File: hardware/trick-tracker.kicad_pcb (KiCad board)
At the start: 2 copper layers, 23.7 x 49.9 mm, 44 parts, among them J1 USB4105-GF-A, J2 S2B-PH-K, J3 QWiiC, U1 MS88SF2, U2 DPS368XTSA1, U3 LSM9DS1, U4 MCP73831-2-OT, U5 MIC5504-3.3YM5

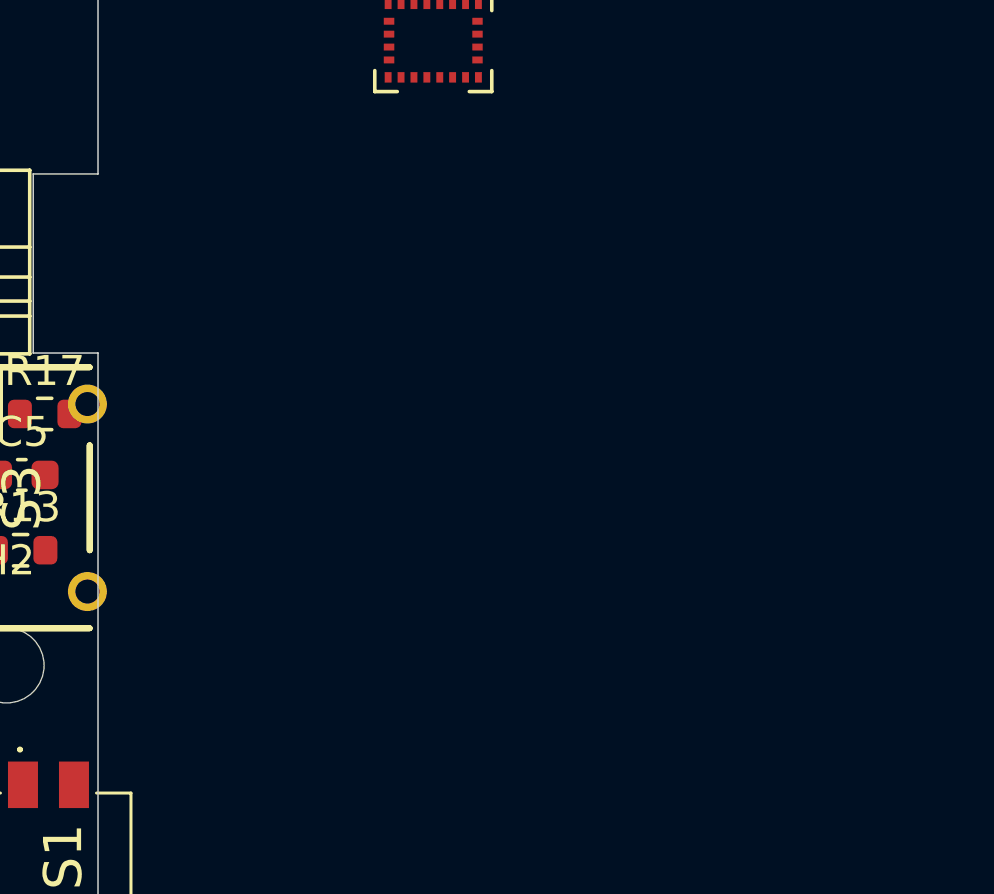
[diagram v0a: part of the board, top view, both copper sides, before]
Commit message: Add Micro SD-Card holder
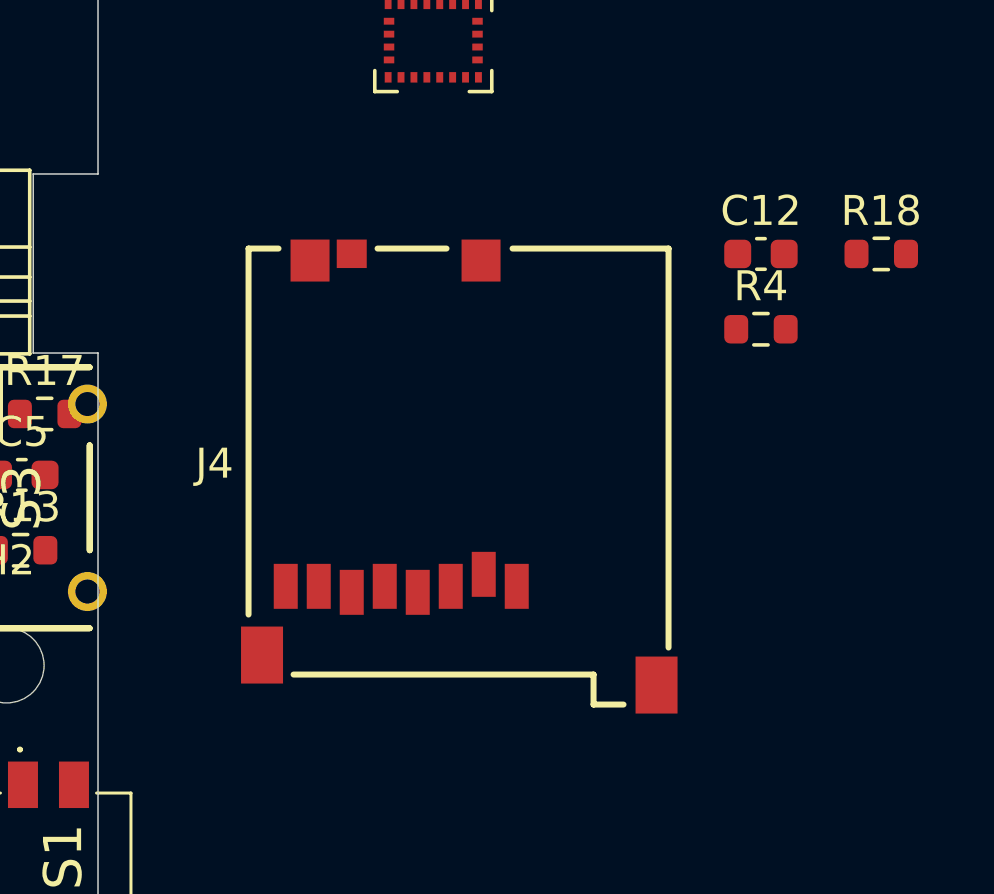
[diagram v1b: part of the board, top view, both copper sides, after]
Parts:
- added C12: 0.1µF, Capacitor_SMD:C_0603_1608Metric, F.Cu at (178.7, 113.0)
- added J4: MEM2051-00-195-00-A, MEM2051-00-195-00-A:GCT_MEM2051-00-195-00-A, F.Cu at (168.6, 120.5)
- added R18: 2M, Resistor_SMD:R_0603_1608Metric, F.Cu at (182.7, 113.0)
- added R4: 806k, Resistor_SMD:R_0603_1608Metric, F.Cu at (178.7, 115.5)
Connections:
- net /CC1 renamed Net-(J1-PadA5)
- net /CC2 renamed Net-(J1-PadB5)
- U1 pad 22: Net-(U1-Pad22) -> /BAT_SENS

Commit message: Moved components
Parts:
- removed LED1: APHF1608LSEEQBDZGKC, APHF1608LSEEQBDZGKC:APHF1608LSEEQBDZGKC
- removed R8: 2k2, Resistor_SMD:R_0603_1608Metric
- removed R9: 390R, Resistor_SMD:R_0603_1608Metric
- added D4: GREEN, LED_SMD:LED_0603_1608Metric, F.Cu at (160.0, 106.7)
- added D5: DSS13UTR, Diode_SMD:D_SOD-123F, F.Cu at (150.0, 122.6)
- added H3: MountingHole, MountingHole:MountingHole_2.5mm, F.Cu at (132.8, 101.3)
- added H4: MountingHole, MountingHole:MountingHole_2.5mm, F.Cu at (158.2, 101.3)
- D1: value MBR120 -> DSS13UTR; footprint Diode_SMD:D_0603_1608Metric -> Diode_SMD:D_SOD-123F
- J4: moved to B.Cu
- R7: value 1k2 -> 470
- U4: value MCP73831-2-OT -> MCP73831/OT
- moved R18 42.5 mm to (140.3, 110.1), turned to 180 degrees
- moved C12 38.6 mm to (140.3, 108.5)
- moved R4 38.5 mm to (140.3, 111.8), turned to 180 degrees
- moved R7 31.2 mm to (158.4, 106.7), turned to 90 degrees
- moved C1 29.6 mm to (152.8, 121.9)
- moved U3 21.5 mm to (146.6, 109.3)
- moved C7 20.2 mm to (149.4, 106.7)
- moved U2 19.5 mm to (135.3, 114.8), turned to 90 degrees
- moved H1 19.3 mm to (132.8, 134.2)
- moved J4 16.8 mm to (152.0, 123.1), turned to 270 degrees
- moved C8 16.3 mm to (146.3, 106.7)
- moved C10 16.1 mm to (132.8, 114.8), turned to 90 degrees
- moved C6 15.4 mm to (147.1, 105.0)
- moved R10 15.3 mm to (146.8, 112.8), turned to 90 degrees
- moved R11 15.0 mm to (143.5, 112.8), turned to 90 degrees
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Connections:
- C1 pad 1: /VBUS -> /VIN
- D1 pad 1: /VBUS -> /VIN
- J4 pad 2: Net-(J4-Pad2) -> /CS
- J4 pad 3: Net-(J4-Pad3) -> /MOSI
- J4 pad 4: Net-(J4-Pad4) -> /3.3V
- J4 pad 5: Net-(J4-Pad5) -> /SCK
- J4 pad 6: Net-(J4-Pad6) -> GND
- J4 pad 7: Net-(J4-Pad7) -> /MISO
- J4 pad 9: Net-(J4-Pad9) -> /SD_DETECT
- R7 pad 1: /LED_RED -> GND
- S3 pad 3: /VBUS -> /VIN
- U1 pad 10: /LED_BLUE -> /MOSI
- U1 pad 16: /NFC1 -> /SD_DETECT
- U1 pad 21: Net-(U1-Pad21) -> /CS
- U1 pad 24: Net-(U1-Pad24) -> /SCK
- U1 pad 8: /LED_RED -> /MISO
- U1 pad 9: /LED_GREEN -> Net-(D4-Pad2)
- U5 pad 1: /VBUS -> /VIN
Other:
- board size 23.7 x 49.9 mm -> 31 x 38.5 mm

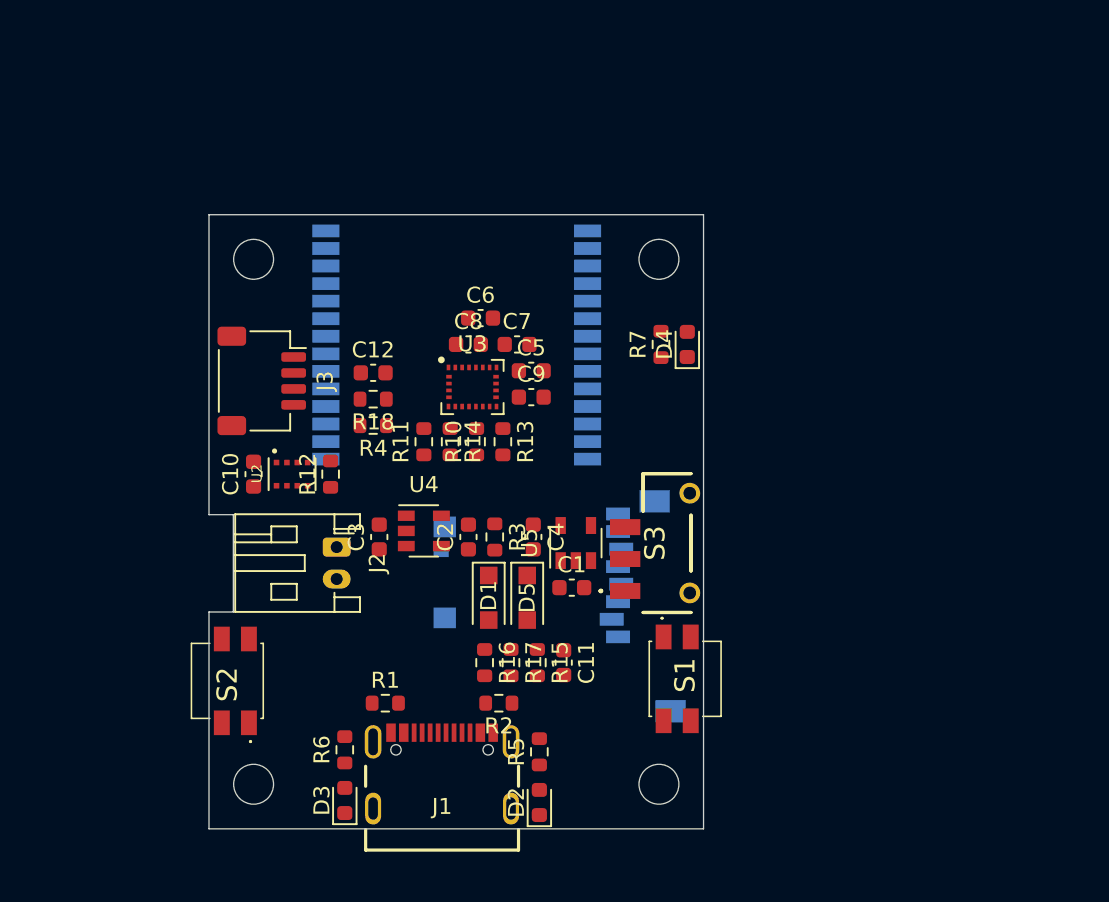
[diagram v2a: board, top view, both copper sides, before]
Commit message: Exchanged battery connector with SMD version
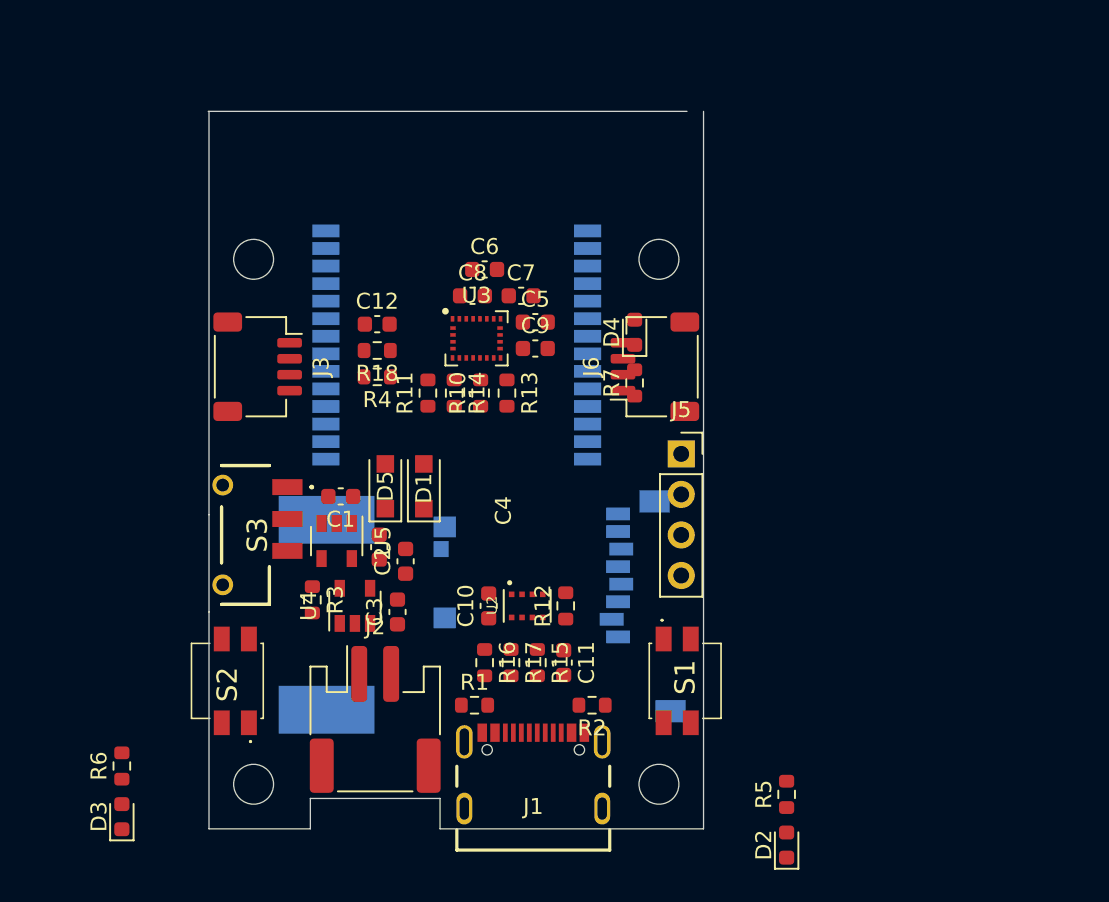
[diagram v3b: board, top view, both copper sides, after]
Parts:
- added J5: Debug, Connector_PinSocket_2.54mm:PinSocket_1x04_P2.54mm_Vertical, F.Cu at (159.6, 113.5)
- added J6: QWiiC, Connector_JST:JST_SH_SM04B-SRSS-TB_1x04-1MP_P1.00mm_Horizontal, F.Cu at (158.0, 108.1)
- added P1: SMTB-1240-S-R, SMTB-1240-S-R:SMTB-1240-S-R, B.Cu at (137.4, 123.6)
- J2: footprint Connector_JST:JST_PH_S2B-PH-K_1x02_P2.00mm_Horizontal -> Connector_JST:JST_PH_S2B-PH-SM4-TB_1x02-1MP_P2.00mm_Horizontal
- R5, R6: value 470 -> 1k
- moved S3 26.4 mm to (132.3, 118.6), turned to 270 degrees
- moved C10 16.9 mm to (147.6, 123.1)
- moved R12 16.9 mm to (152.4, 123.1)
- moved U2 16.9 mm to (150.0, 123.1)
- moved D2 15.7 mm to (166.2, 138.0)
- moved R5 15.7 mm to (166.2, 134.9)
- moved C1 15.6 mm to (138.3, 116.2), turned to 180 degrees
- moved U5 15.0 mm to (138.0, 119.0), turned to 270 degrees
- moved D3 14.0 mm to (124.6, 136.3)
- moved R6 14.0 mm to (124.6, 133.1)
- moved R3 12.1 mm to (136.5, 122.7)
- moved D5 11.3 mm to (141.1, 115.6), turned to 90 degrees
- moved J2 11.1 mm to (140.5, 130.2), turned to 0 degrees
- moved C4 9.67 mm to (140.7, 119.4), turned to 90 degrees
- moved D1 8.08 mm to (143.5, 115.6), turned to 90 degrees
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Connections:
- U1 pad 15: /NFC2 -> Net-(P1-Pad1)
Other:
- board size 31 x 38.5 mm -> 31 x 45 mm

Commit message: Add ESD protection for USB
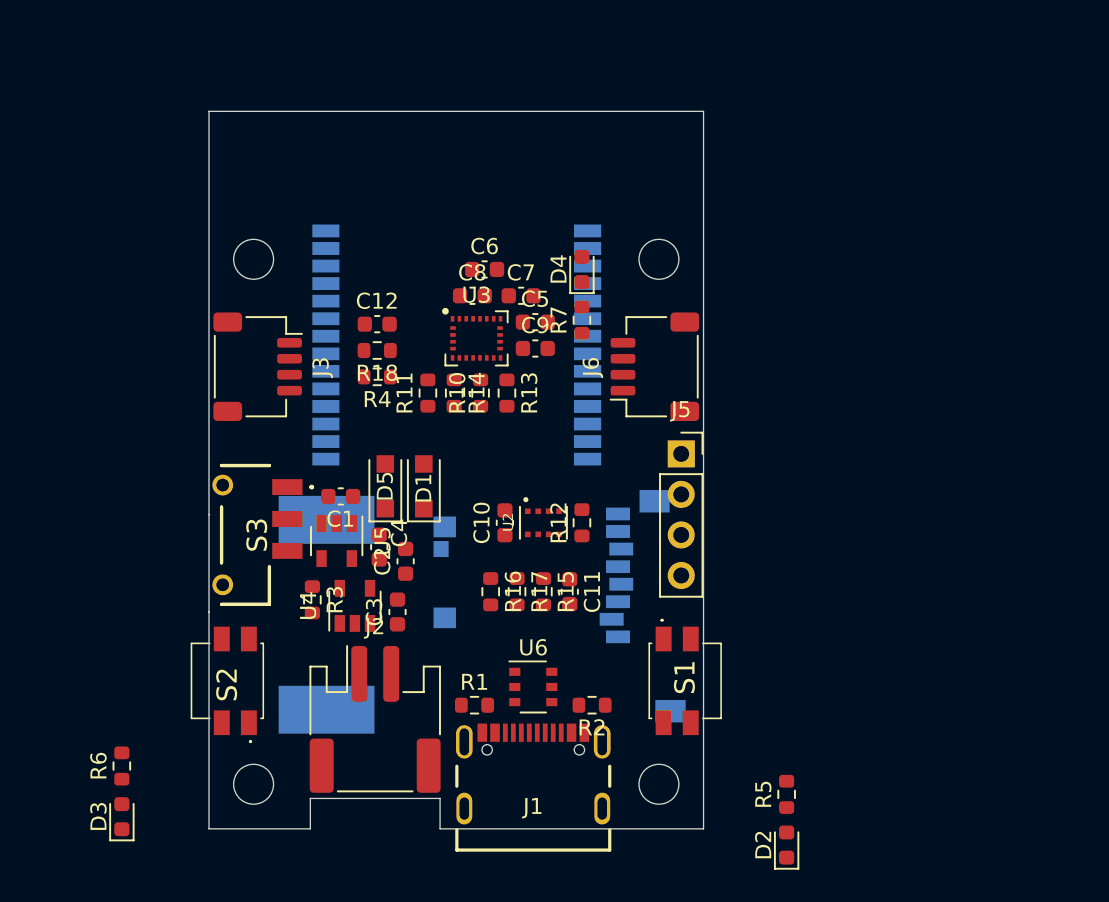
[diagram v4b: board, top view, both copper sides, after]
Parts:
- added U6: IP4220CZ6, Package_SO:TSOP-6_1.65x3.05mm_P0.95mm, F.Cu at (150.4, 128.1)
- moved C10 5.31 mm to (148.6, 117.9)
- moved R12 5.31 mm to (153.4, 117.9)
- moved U2 5.31 mm to (151.0, 117.9)
- moved D4 5.14 mm to (153.4, 102.0)
- moved R7 5.14 mm to (153.4, 105.2)
- moved C11 4.46 mm to (152.7, 122.2)
- moved R16 4.46 mm to (147.7, 122.2)
- moved R17 4.46 mm to (149.4, 122.2)
- moved R15 4.46 mm to (151.0, 122.2)
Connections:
- U1 pad 22: /BAT_SENS -> /INT1_AG
- U1 pad 6: /INT1_AG -> /BAT_SENS
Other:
- outline, holes or cut-outs redrawn

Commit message: Exchanged SD Card holder with one which can be hand-soldered
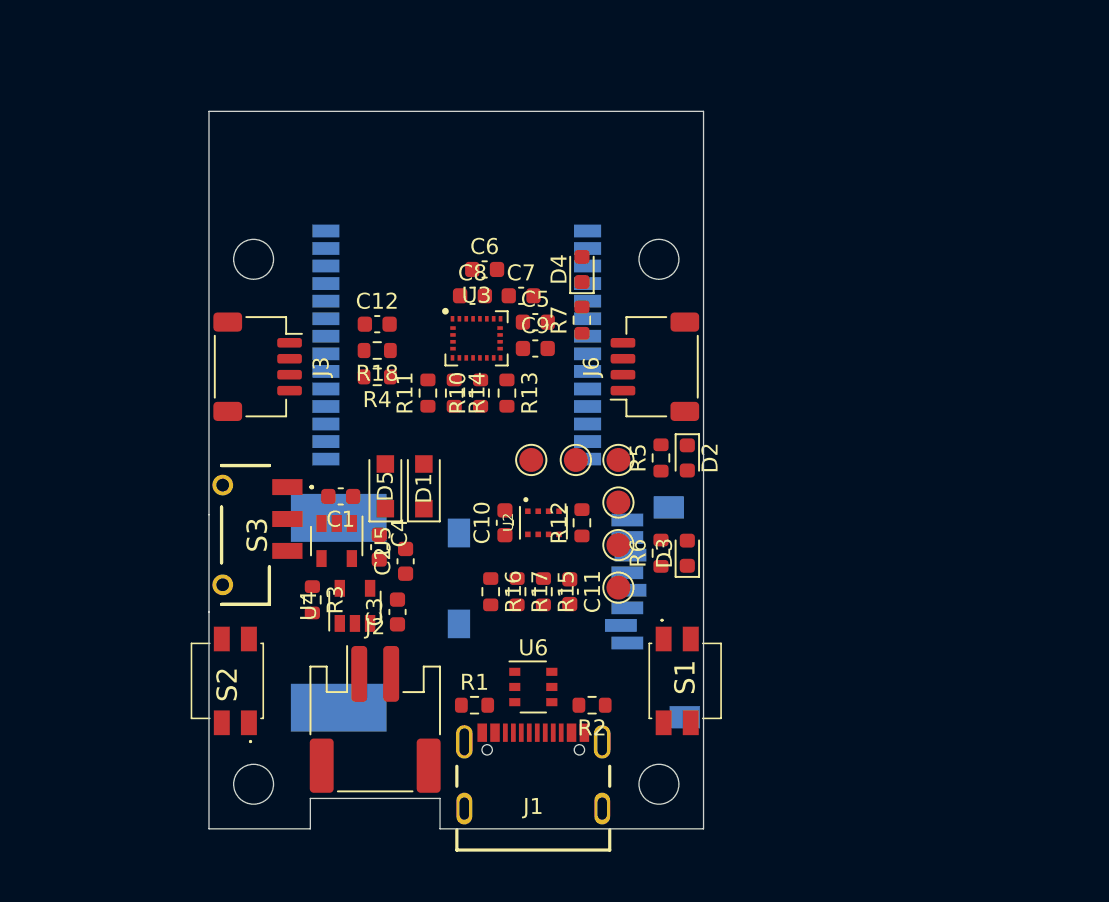
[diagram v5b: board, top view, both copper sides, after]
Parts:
- removed J5: Debug, Connector_PinSocket_2.54mm:PinSocket_1x04_P2.54mm_Vertical
- added TP1: TP_Tx, TestPoint:TestPoint_Pad_D1.5mm, F.Cu at (153.0, 113.9)
- added TP2: TP_Rx, TestPoint:TestPoint_Pad_D1.5mm, F.Cu at (150.2, 113.9)
- added TP3: TP_SWDCLK, TestPoint:TestPoint_Pad_D1.5mm, F.Cu at (155.7, 113.9)
- added TP4: TP_SWD, TestPoint:TestPoint_Pad_D1.5mm, F.Cu at (155.7, 116.6)
- added TP5: TP_3v3, TestPoint:TestPoint_Pad_D1.5mm, F.Cu at (155.7, 119.3)
- added TP6: TP_GND, TestPoint:TestPoint_Pad_D1.5mm, F.Cu at (155.7, 121.9)
- J4: footprint MEM2051-00-195-00-A:GCT_MEM2051-00-195-00-A -> MEM2061-01-188-00-A_REVA:GCT_MEM2061-01-188-00-A_REVA
- moved D3 39.1 mm to (160.0, 119.8)
- moved R6 36.3 mm to (158.4, 119.8)
- moved D2 25.0 mm to (160.0, 113.8), turned to 270 degrees
- moved R5 22.5 mm to (158.4, 113.8)
- moved J4 1.09 mm to (153.0, 123.4)
- moved P1 0.77 mm to (138.2, 123.4)

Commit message: Started layouting
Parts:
- moved S1 27.7 mm to (131.7, 127.8), turned to 270 degrees
- moved S2 27.7 mm to (159.4, 127.8), turned to 90 degrees
- moved C12 9.72 mm to (143.9, 114.6), turned to 90 degrees
- moved R18 8.98 mm to (145.5, 114.6), turned to 270 degrees
- moved R4 8.82 mm to (147.2, 114.6), turned to 270 degrees
- moved D1 7.17 mm to (144.4, 122.7), turned to 270 degrees
- moved C6 1.82 mm to (146.6, 103.6)
- moved R10 1.82 mm to (146.3, 111.4)
- moved R11 1.82 mm to (143.0, 111.4)
- moved R13 1.82 mm to (148.0, 111.4)
- moved R14 1.82 mm to (144.7, 111.4)
- moved C5 1.82 mm to (149.7, 106.9)
- moved C7 1.82 mm to (148.8, 105.3)
- moved C8 1.82 mm to (145.8, 105.3)
- moved C9 1.82 mm to (149.7, 108.6)
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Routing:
- net /D+: track 0.00 -> 76.1 mm, vias 0 -> 1
- net /D-: track 0.00 -> 73.9 mm, vias 0 -> 1
- net /VBUS: track 0.00 -> 48.1 mm
- net GND: track 0.00 -> 29.7 mm, vias 0 -> 25
- net /STAT: track 0.00 -> 10.6 mm, vias 0 -> 2
- net /VBAT: track 0.00 -> 7.78 mm
- net Net-(J1-PadA5): track 0.00 -> 3.91 mm, vias 0 -> 2
- net /EN: track 0.00 -> 2.80 mm
- net Net-(J1-PadB5): track 0.00 -> 2.30 mm
- net Net-(D3-Pad2): track 0.00 -> 1.67 mm
- net Net-(D2-Pad1): track 0.00 -> 1.67 mm
- net Net-(D4-Pad1): track 0.00 -> 1.56 mm
- added copper zone on F.Cu, net /3.3V
- added copper zone on F.Cu, net /VIN
- added copper zone on B.Cu, net GND

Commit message: Finished trace routing
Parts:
- J4: value MEM2051-00-195-00-A -> MEM2061-01-188-00-A
- moved TP6 23.7 mm to (146.8, 99.9), turned to 90 degrees
- moved TP5 22.5 mm to (144.1, 99.9), turned to 90 degrees
- moved TP3 21.9 mm to (138.8, 99.9), turned to 90 degrees
- moved TP4 21.9 mm to (141.5, 99.9), turned to 90 degrees
- moved TP1 14.0 mm to (152.3, 99.9)
- moved TP2 14.0 mm to (149.5, 99.9)
- moved D4 12.3 mm to (156.7, 113.8)
- moved R7 8.79 mm to (155.1, 113.8)
- moved R4 3.95 mm to (143.3, 114.8), turned to 90 degrees
- moved C12 3.19 mm to (147.1, 114.8), turned to 270 degrees
- moved R10 1.65 mm to (144.7, 111.4)
- moved R11 1.65 mm to (141.4, 111.4)
- moved R13 1.65 mm to (146.3, 111.4)
- moved R14 1.65 mm to (143.0, 111.4)
- moved R18 0.46 mm to (145.2, 114.8), turned to 90 degrees
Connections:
- J1 pad S2: Net-(J1-PadS1) -> Net-(J1-PadS2)
- J1 pad S3: Net-(J1-PadS1) -> Net-(J1-PadS3)
- J1 pad S4: Net-(J1-PadS1) -> Net-(J1-PadS4)
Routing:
- net /SCL: track 0.00 -> 60.3 mm, vias 0 -> 2
- net /SDA: track 0.00 -> 56.6 mm, vias 0 -> 3
- net /RESET: track 0.00 -> 51.0 mm, vias 0 -> 3
- net /CS: track 0.00 -> 41.9 mm, vias 0 -> 2
- net /D+: track 76.1 -> 37.1 mm
- net /D-: track 73.9 -> 35.0 mm
- net Net-(P1-Pad1): track 0.00 -> 34.9 mm
- net /PRESS_INT: track 0.00 -> 33.2 mm, vias 0 -> 1
- net /BTN: track 0.00 -> 32.6 mm, vias 0 -> 3
- net /STAT: track 10.6 -> 42.1 mm, vias 2 -> 4
- net /3.3V: track 0.00 -> 29.4 mm, vias 0 -> 24
- net /SCK: track 0.00 -> 25.2 mm
- net /SD_DETECT: track 0.00 -> 23.3 mm, vias 0 -> 2
- net GND: track 29.7 -> 52.7 mm, vias 25 -> 47
- net /MOSI: track 0.00 -> 20.3 mm
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- added copper zone on F.Cu, net (none)
- added copper zone on In2.Cu, net /3.3V
- added copper zone on In2.Cu, net /VBAT
- added copper zone on In2.Cu, net /VBUS
- added copper zone on In2.Cu, net /VIN
- added copper zone on In1.Cu, net GND
- removed copper zone on F.Cu, net /3.3V
- removed copper zone on F.Cu, net /VIN
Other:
- copper layers 2 -> 4
